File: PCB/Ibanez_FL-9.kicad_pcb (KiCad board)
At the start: 2 copper layers, 60 x 77 mm, 154 parts, among them J3 EXT_DC, Q101 2SC2458GR, Q102 2SC2458GR, Q103 2SK44SPC, Q104 2SC2458GR, Q105 2SC2458GR, Q106 2SC2458GR, Q107 2SA1048Y/GR, Q108A1001 2SC1583F, Q108B1001 2SC1583F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

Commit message: update pcb layout
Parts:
- added R143: 1M, Resistor_THT:R_Axial_DIN0204_L3.6mm_D1.6mm_P2.54mm_Vertical, F.Cu at (196.5, 86.7)
- C113, C119: footprint Capacitor_THT:C_Rect_L7.0mm_W2.5mm_P5.00mm -> Capacitor_THT:C_Rect_L7.0mm_W2.0mm_P5.00mm
- Q101, Q102, Q103, Q104, Q105, Q106, Q107, Q108A1001, Q108B1001, Q109: footprint Package_TO_SOT_THT:TO-92_Inline -> Package_TO_SOT_THT:TO-92Flat
- moved R106 124.3 mm to (229.7, 76.0), turned to 180 degrees
- moved C119 120.7 mm to (213.5, 90.5)
- moved C113 114.8 mm to (205.5, 78.0), turned to 90 degrees
- moved R120 101.5 mm to (220.3, 76.0)
- moved C118 98.3 mm to (214.8, 87.5)
- moved R201 95.8 mm to (200.0, 94.0), turned to 90 degrees
- moved R202 94.9 mm to (199.0, 98.7), turned to 90 degrees
- moved C201 92.5 mm to (202.0, 91.8), turned to -90 degrees
- moved R127 92.0 mm to (217.5, 80.3), turned to -90 degrees
- moved C202 91.6 mm to (201.0, 96.2), turned to -90 degrees
- moved R126 90.2 mm to (213.4, 85.9), turned to 135 degrees
- moved R124 90.0 mm to (212.7, 79.5), turned to 180 degrees
- moved R125 89.6 mm to (212.7, 82.0), turned to 180 degrees
- moved R129 88.5 mm to (215.0, 81.0), turned to -90 degrees
- moved R128 87.4 mm to (211.0, 92.2), turned to 90 degrees
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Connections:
- Q106 pad 3: Net-(C202-Pad1) -> Net-(Q106-Pad3)
- R106 pad 1: /4.5v -> Net-(R106-Pad1)
- R106 pad 2: Net-(R106-Pad2) -> /4.5v
- R120 pad 1: /4.5v -> Net-(U102-Pad3)
- R120 pad 2: Net-(R120-Pad2) -> /4.5v
- R123 pad 1: GND -> /CP12
- R123 pad 2: /CP12 -> GND
- R127 pad 1: Net-(C118-Pad1) -> /CP4
- R127 pad 2: /CP4 -> Net-(C118-Pad1)
- R129 pad 1: /CP15 -> Net-(C118-Pad1)
- R129 pad 2: Net-(C118-Pad1) -> /CP15
- U102 pad 3: Net-(R120-Pad2) -> Net-(U102-Pad3)
- U102 pad 5: Net-(R106-Pad2) -> Net-(R106-Pad1)
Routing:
- net /CP1: track 0.00 -> 9.80 mm, vias 0 -> 2
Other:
- board text added: "CR1"
- board text added: "CR2"
- board text added: "IBANEZ FL9 FLANGER 1985"

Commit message: pcb layout v1.0
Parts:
- removed BT1: 9V Battery, Battery:BatteryHolder_MPD_BA9VPC_1xPP3
- removed D1: LN21CPSL, LED_THT:LED_D3.0mm_Clear
- removed RV1: 500K, Potentiometer_THT:Potentiometer_ACP_CA6-H2,5_Horizontal
- removed RV2: 100K, Potentiometer_THT:Potentiometer_ACP_CA6-H2,5_Horizontal
- removed RV3: 50K, Potentiometer_THT:Potentiometer_ACP_CA6-H2,5_Horizontal
- removed RV4: 10K, Potentiometer_THT:Potentiometer_ACP_CA6-H2,5_Horizontal
- removed SW1: NORMAL/EFFECT, Button_Switch_THT:SW_PUSH-12mm
- C111: footprint Capacitor_THT:C_Rect_L7.0mm_W2.5mm_P5.00mm -> Capacitor_THT:C_Rect_L7.0mm_W2.0mm_P5.00mm
- C112: value 0.001uf CER -> 0.001uf FILM; footprint Capacitor_THT:C_Disc_D3.0mm_W2.0mm_P2.50mm -> Capacitor_THT:C_Rect_L7.0mm_W2.0mm_P5.00mm
- C129: value 0.01uf -> 0.01uf FILM; footprint Capacitor_THT:C_Disc_D3.0mm_W2.0mm_P2.50mm -> Capacitor_THT:C_Rect_L7.0mm_W2.0mm_P5.00mm
- D105: footprint Diode_THT:D_DO-15_P2.54mm_Vertical_KathodeUp -> Diode_THT:D_T-1_P2.54mm_Vertical_KathodeUp
- moved R118 96.3 mm to (213.3, 69.0)
- moved R119 93.8 mm to (210.8, 71.0)
- moved R117 93.5 mm to (210.5, 64.8), turned to -90 degrees
- moved C111 87.0 mm to (213.5, 73.0)
- moved R121 85.2 mm to (208.5, 65.0), turned to -90 degrees
- moved R140 83.8 mm to (195.0, 104.7), turned to 90 degrees
- moved R141 81.3 mm to (192.3, 107.5)
- moved R122 79.7 mm to (203.3, 67.0)
- moved R133 78.7 mm to (203.7, 88.0), turned to 180 degrees
- moved C121 74.9 mm to (199.0, 85.5)
- moved C112 73.9 mm to (218.5, 70.5), turned to 90 degrees
- moved R139 69.0 mm to (197.0, 104.2), turned to 90 degrees
- moved R144 68.9 mm to (189.5, 106.3), turned to -90 degrees
- moved R135 68.5 mm to (189.8, 98.5)
- moved R134 67.3 mm to (189.8, 92.5)
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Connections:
- C110 pad 2: Net-(C110-Pad2) -> Net-(R117-Pad1)
- R117 pad 1: Net-(C111-Pad2) -> Net-(R117-Pad1)
- R117 pad 2: Net-(C110-Pad2) -> Net-(C111-Pad2)
- R118 pad 1: Net-(C112-Pad1) -> Net-(C111-Pad2)
- R118 pad 2: Net-(C111-Pad2) -> Net-(C112-Pad1)
- R134 pad 1: Net-(C202-Pad1) -> +9V
- R134 pad 2: +9V -> Net-(C202-Pad1)
- R135 pad 1: Net-(C201-Pad2) -> +9V
- R135 pad 2: +9V -> Net-(C201-Pad2)
- R140 pad 1: GND -> Net-(R138-Pad1)
- R140 pad 2: Net-(R138-Pad1) -> GND
- R141 pad 1: Net-(JP11-Pad1) -> Net-(C122-Pad1)
- R141 pad 2: Net-(C122-Pad1) -> Net-(JP11-Pad1)
- R149 pad 1: Net-(C128-Pad1) -> Net-(Q108A1001-Pad2)
- R149 pad 2: Net-(Q108A1001-Pad2) -> Net-(C128-Pad1)
- R155 pad 1: Net-(C129-Pad2) -> Net-(R156-Pad2)
- R155 pad 2: Net-(R155-Pad2) -> Net-(C129-Pad2)
- R156 pad 1: Net-(R155-Pad2) -> Net-(C131-Pad2)
- R156 pad 2: Net-(C131-Pad2) -> Net-(R156-Pad2)
- U103 pad 3: Net-(R155-Pad2) -> Net-(R156-Pad2)
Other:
- board text added: "LED ANODE"
- board text added: "LED CATHODE"

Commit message: add custom components; fix all labels
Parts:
- removed Q108A1001, Q108B1001: 2SC1583F, Package_TO_SOT_THT:TO-92Flat
- added Q108: 2SC1583F, Package_TO_SOT_THT:TO-92Flat_5-PIN, F.Cu at (188.9, 53.9)
- moved C133 0.98 mm to (225.0, 104.8)
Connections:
- net Net-(C121-Pad2) renamed /CP14
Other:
- board text added: "CP10 +9V"
- board text added: "CP12"
- board text added: "CP13"
- board text added: "CP14"
- board text added: "CP2 +4.5V"
- board text added: "CP3 +5V"
- board text added: "CP6"

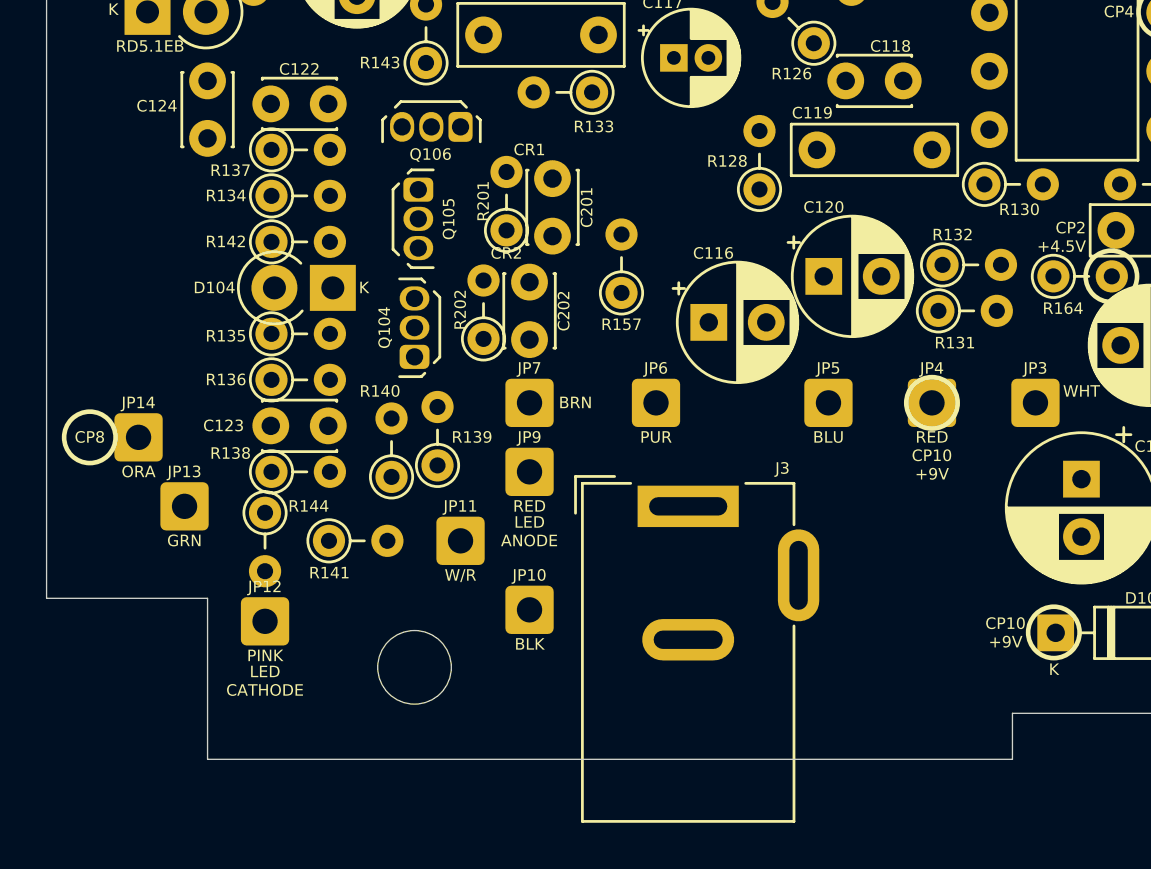
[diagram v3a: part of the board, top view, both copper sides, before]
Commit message: update test points; add hybrid devices
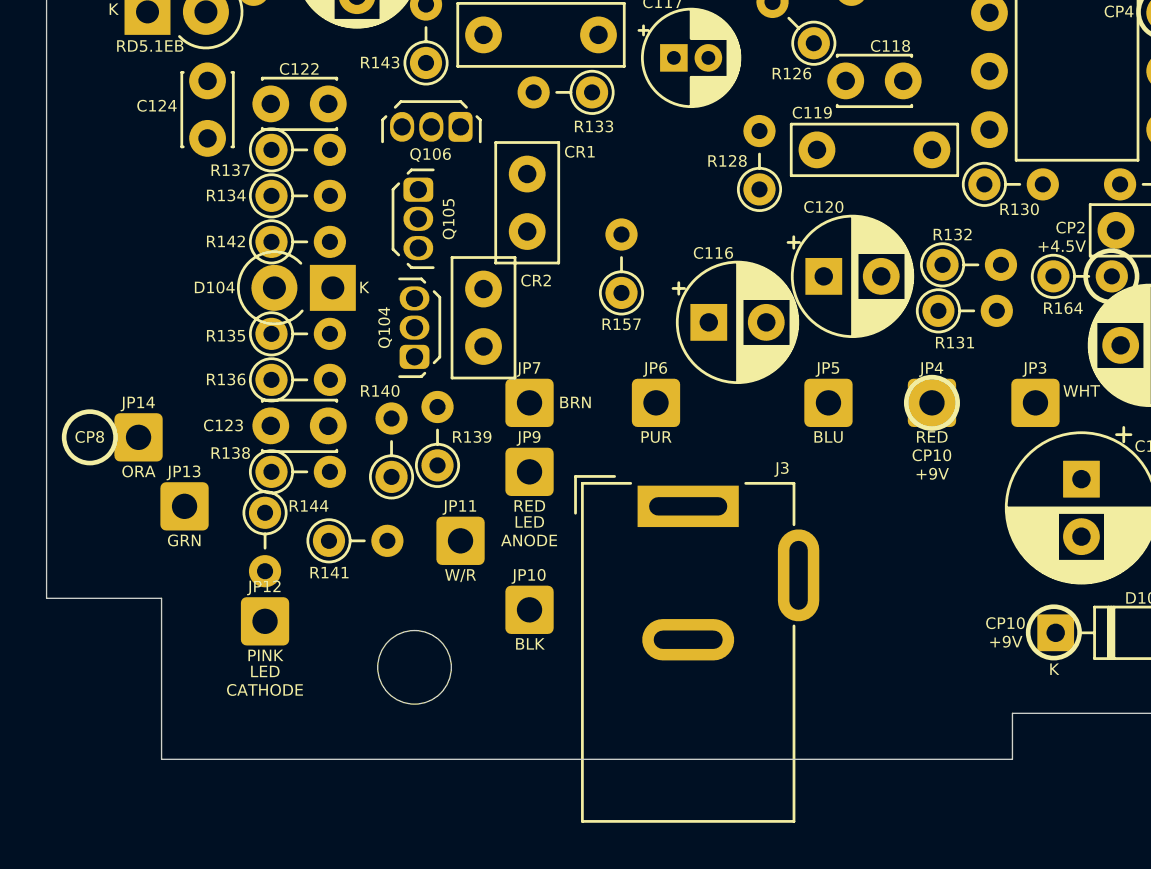
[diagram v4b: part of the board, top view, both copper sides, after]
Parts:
- removed C201, C202: 0.001uf CER, Capacitor_THT:C_Disc_D3.0mm_W2.0mm_P2.50mm
- removed R201, R202: 100K, Resistor_THT:R_Axial_DIN0204_L3.6mm_D1.6mm_P2.54mm_Vertical
- added CR1: CR_N01, Capacitor_THT:C_Disc_D5.0mm_W2.5mm_P2.50mm, F.Cu at (200.9, 91.5)
- added CR2: CR_N01, Capacitor_THT:C_Disc_D5.0mm_W2.5mm_P2.50mm, F.Cu at (199.0, 96.5)
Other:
- outline, holes or cut-outs redrawn
- board text removed: "CR1"
- board text removed: "CR2"

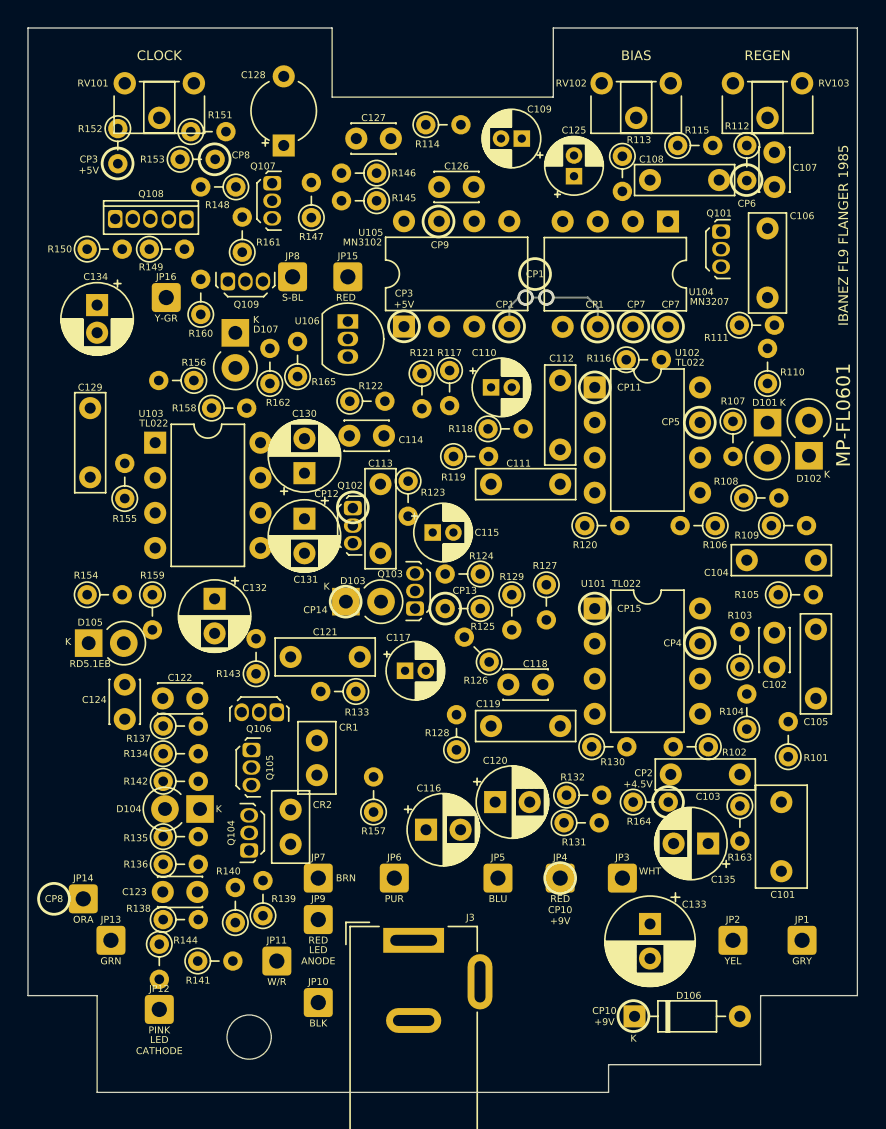
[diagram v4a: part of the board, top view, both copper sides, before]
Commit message: update board layout and docs
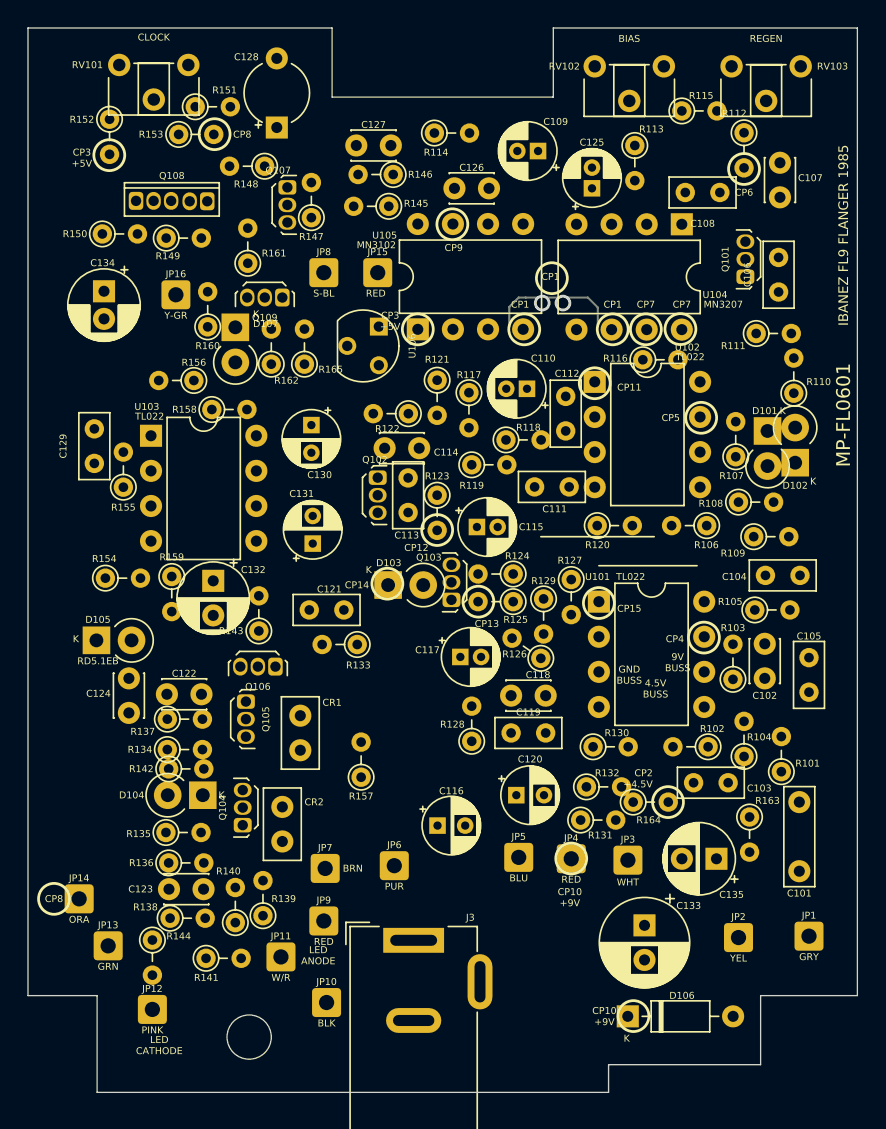
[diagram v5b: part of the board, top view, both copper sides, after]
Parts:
- added G***: FL-9_PCB_TOP_orig_legend_2, CedarGrove_custom:FL-9_PCB_TOP_orig_legend_2, F.Cu at (210.2, 78.2)
- added G***: FL-9_PCB_BOT_traces_neg, CedarGrove_custom:FL-9_PCB_BOT_traces_neg, B.Cu at (210.0, 78.5)
- C101: footprint Capacitor_THT:C_Rect_L7.2mm_W3.5mm_P5.00mm_FKS2_FKP2_MKS2_MKP2 -> Capacitor_THT:C_Rect_L7.0mm_W2.0mm_P5.00mm
- C103, C104, C105, C108, C111, C112, C113, C119, C129: footprint Capacitor_THT:C_Rect_L7.0mm_W2.0mm_P5.00mm -> Capacitor_THT:C_Rect_L4.6mm_W2.0mm_P2.50mm_MKS02_FKP02
- C106, C121: footprint Capacitor_THT:C_Rect_L7.0mm_W2.5mm_P5.00mm -> Capacitor_THT:C_Rect_L4.6mm_W2.0mm_P2.50mm_MKS02_FKP02
- C116, C120: footprint Capacitor_THT:CP_Radial_D5.0mm_P2.50mm -> Capacitor_THT:CP_Radial_D4.0mm_P2.00mm
- C130: renamed from C131; footprint Capacitor_THT:CP_Radial_D5.0mm_P2.50mm -> Capacitor_THT:CP_Radial_D4.0mm_P2.00mm
- C131: renamed from C130; footprint Capacitor_THT:CP_Radial_D5.0mm_P2.50mm -> Capacitor_THT:CP_Radial_D4.0mm_P2.00mm
- D101, D102, D103, D104, D107: value 1N4004 -> 1N4148
- U106: footprint Package_TO_SOT_THT:TO-92_Inline -> Package_TO_SOT_THT:TO-92
- moved C130 6.79 mm to (200.5, 68.7)
- moved C113 5.81 mm to (207.5, 72.5), turned to -90 degrees
- moved C131 5.13 mm to (200.6, 77.3)
- moved R122 4.33 mm to (207.5, 67.9), turned to 180 degrees
- moved C117 4.12 mm to (211.3, 85.5)
- moved Q109 4.11 mm to (198.4, 59.5), turned to 180 degrees
- moved R126 3.75 mm to (217.1, 85.6), turned to 145 degrees
- moved Q101 3.71 mm to (231.9, 58.0), turned to 90 degrees
- moved C121 3.66 mm to (200.3, 82.1)
- moved Q105 3.52 mm to (195.8, 88.7)
- moved R133 3.40 mm to (203.8, 84.6)
- moved Q106 3.30 mm to (197.9, 86.2)
- moved D103 3.28 mm to (206.1, 80.3)
- moved C115 3.22 mm to (212.5, 76.1)
- moved C111 3.16 mm to (216.7, 73.2)
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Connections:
- C130 pad 2: Net-(C131-Pad2) -> Net-(C130-Pad2)
- C131 pad 1: Net-(C130-Pad1) -> Net-(C131-Pad1)
- Q101 pad 1: /CP6 -> Net-(C107-Pad2)
- Q101 pad 3: Net-(C107-Pad2) -> /CP6
- Q102 pad 1: /CP12 -> Net-(C114-Pad2)
- Q102 pad 3: Net-(C114-Pad2) -> /CP12
- Q104 pad 1: Net-(D104-Pad2) -> Net-(C123-Pad2)
- Q104 pad 3: Net-(C123-Pad2) -> Net-(D104-Pad2)
- Q105 pad 1: Net-(D104-Pad2) -> Net-(C122-Pad2)
- Q105 pad 3: Net-(C122-Pad2) -> Net-(D104-Pad2)
- Q106 pad 1: Net-(D104-Pad2) -> Net-(Q106-Pad1)
- Q106 pad 3: Net-(Q106-Pad3) -> Net-(D104-Pad2)
- Q109 pad 1: Net-(JP8-Pad2) -> Net-(D107-Pad1)
- Q109 pad 3: Net-(D107-Pad1) -> Net-(JP8-Pad2)
- R107 pad 1: /CP5 -> Net-(C104-Pad2)
- R107 pad 2: Net-(C104-Pad2) -> /CP5
- R116 pad 1: GND -> /CP7
- R116 pad 2: /CP7 -> GND
- R122 pad 1: Net-(C114-Pad2) -> Net-(C113-Pad1)
- R122 pad 2: Net-(C113-Pad1) -> Net-(C114-Pad2)
- R123 pad 1: /CP12 -> GND
- R123 pad 2: GND -> /CP12
- R143 pad 1: Net-(Q106-Pad3) -> Net-(Q106-Pad1)
- R156 pad 1: Net-(C131-Pad2) -> Net-(C130-Pad1)
- R157 pad 1: Net-(C130-Pad2) -> Net-(C131-Pad1)
- R159 pad 1: GND -> Net-(C132-Pad1)
- R159 pad 2: Net-(C132-Pad1) -> GND
- R163 pad 1: /4.5v -> +9V
- R163 pad 2: +9V -> /4.5v
- U103 pad 6: Net-(C130-Pad2) -> Net-(C131-Pad1)
- U103 pad 7: Net-(C131-Pad2) -> Net-(C130-Pad1)
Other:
- board text added: "4.5V BUSS"
- board text added: "9V BUSS"
- board text added: "GND BUSS"

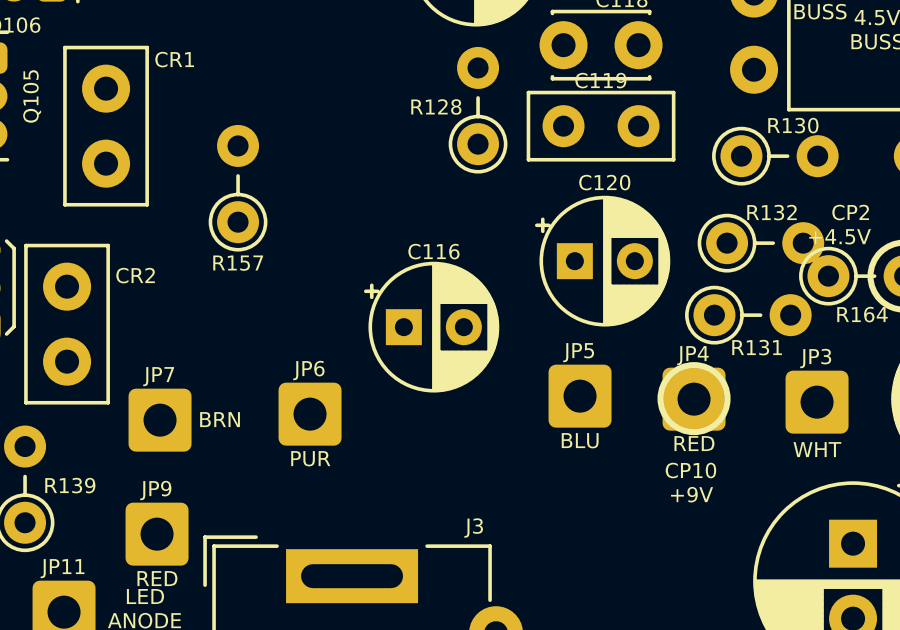
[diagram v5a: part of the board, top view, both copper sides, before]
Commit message: update board layout and docs
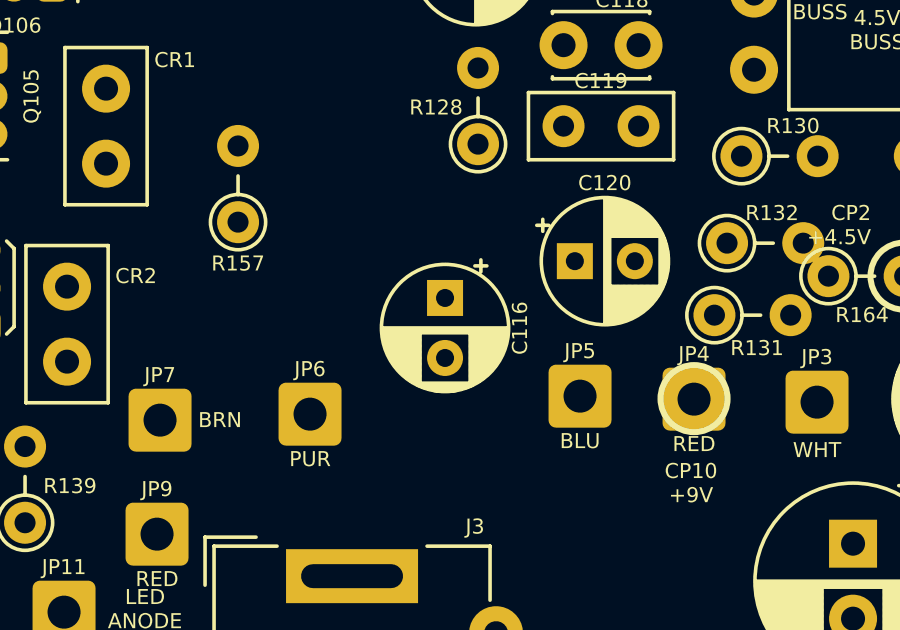
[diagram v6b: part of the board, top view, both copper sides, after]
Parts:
- moved C116 1.68 mm to (211.0, 96.7), turned to -90 degrees
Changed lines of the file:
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@@
   )
   (footprint "Capacitor_THT:CP_Radial_D4.0mm_P2.00mm" locked (layer "F.Cu")
-    (at 209.627401 97.7)
+    (at 211 96.727401 -90)
     (descr "CP, Radial series, Radial, pin pitch=2.00mm, , diameter=4mm, Electrolytic Capacitor")
     (tags "CP Radial series Radial pin pitch 2.00mm  diameter 4mm Electrolytic Capacitor")
@@
     (property "Sheetname" "")
     (attr through_hole)
-    (fp_text reference "C116" (at 1.005112 -2.5) (layer "F.SilkS")
+    (fp_text reference "C116" (at 1.005112 -2.5 90) (layer "F.SilkS")
       (effects (font (size 0.5 0.5) (thickness 0.1)))
     )
-    (fp_text value "0.22uf/50v" (at 1 3.25) (layer "F.Fab")
+    (fp_text value "0.22uf/50v" (at 1 3.25 90) (layer "F.Fab")
       (effects (font (size 0.5 0.5) (thickness 0.1)))
     )
-    (fp_text user "${REFERENCE}" (at 1 0) (layer "F.Fab")
+    (fp_text user "${REFERENCE}" (at 1 0 90) (layer "F.Fab")
       (effects (font (size 0.5 0.5) (thickness 0.1)))
     )
@@
     (fp_line (start -0.702554 -0.8675) (end -0.302554 -0.8675) (layer "F.Fab") (width 0.1))
     (fp_circle (center 1 0) (end 3 0) (layer "F.Fab") (width 0.1) (fill none))
-    (pad "1" thru_hole rect locked (at 0 0) (size 1.2 1.2) (drill 0.6) (layers *.Cu *.Mask)
+    (pad "1" thru_hole rect locked (at 0 0 270) (size 1.2 1.2) (drill 0.6) (layers *.Cu *.Mask)
       (net 25 "/CP13") (pintype "passive"))
-    (pad "2" thru_hole circle locked (at 2 0) (size 1.2 1.2) (drill 0.6) (layers *.Cu *.Mask)
+    (pad "2" thru_hole circle locked (at 2 0 270) (size 1.2 1.2) (drill 0.6) (layers *.Cu *.Mask)
       (net 26 "Net-(C116-Pad2)") (pintype "passive"))
     (model "${KICAD6_3DMODEL_DIR}/Capacitor_THT.3dshapes/CP_Radial_D4.0mm_P2.00mm.wrl"

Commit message: update docs
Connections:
- R153 pad 1: Net-(C128-Pad1) -> /CP8
- R153 pad 2: /CP8 -> Net-(C128-Pad1)
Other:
- board text added: "+BATT"
